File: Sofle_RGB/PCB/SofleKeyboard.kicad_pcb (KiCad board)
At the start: 2 copper layers, 143.4 x 111.8 mm, 97 parts, among them J1 LED, J2 4PIN, J3 OLED, J4 key leds, J5 backlight sel, J6 indicator bypass, P1 i2c_pin, P2 i2c_pin, SW1 SW_PUSH-MX_W_LED, SW10 SW_PUSH-MX_W_LED, SW11 SW_PUSH-MX_W_LED, SW12 SW_PUSH-MX_W_LED, SW13 SW_PUSH-MX_W_LED, SW14 SW_PUSH-MX_W_LED, SW15 SW_PUSH-MX_W_LED, SW16 SW_PUSH-MX_W_LED, SW17 SW_PUSH-MX_W_LED, SW18 SW_PUSH-MX_W_LED, SW19 SW_PUSH-MX_W_LED, SW2 SW_PUSH-MX_W_LED, SW20 SW_PUSH-MX_W_LED, SW21 SW_PUSH-MX_W_LED, SW22 SW_PUSH-MX_W_LED, SW23 SW_PUSH-MX_W_LED, SW24 SW_PUSH-MX_W_LED, SW25 Rotary_Encoder_Switch, SW26 SW_PUSH-MX_W_LED, SW27 SW_PUSH-MX_W_LED, SW28 SW_PUSH-MX_W_LED, SW29 SW_PUSH-MX_W_LED, SW3 SW_PUSH-MX_W_LED, SW30 SW_PUSH-MX_W_LED, SW4 SW_PUSH-MX_W_LED, SW5 SW_PUSH-MX_W_LED, SW6 SW_PUSH-MX_W_LED, SW7 SW_PUSH-MX_W_LED, SW8 SW_PUSH-MX_W_LED, SW9 SW_PUSH-MX_W_LED, U1 ProMicro

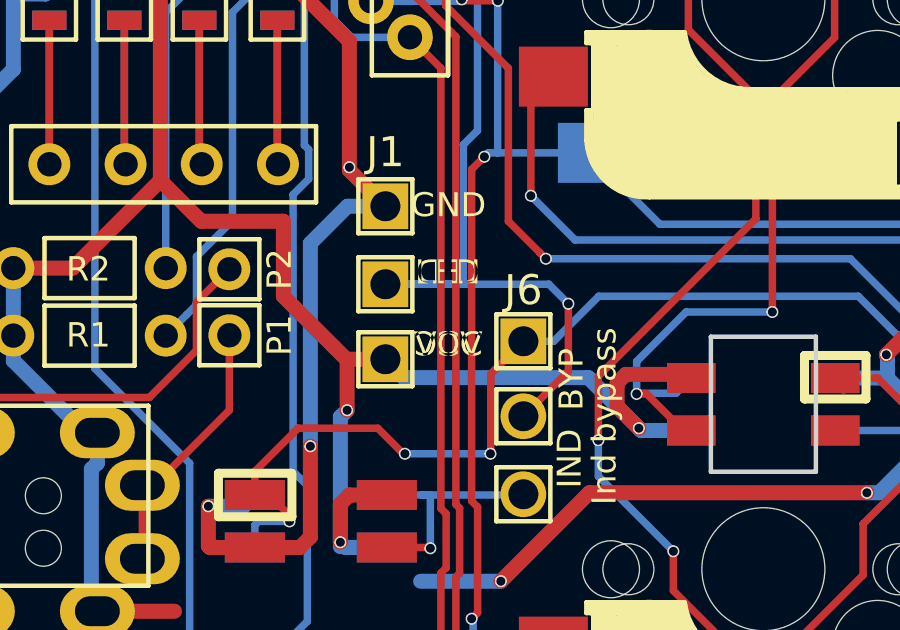
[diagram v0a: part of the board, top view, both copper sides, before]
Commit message: Fix labels for the RGB connector.
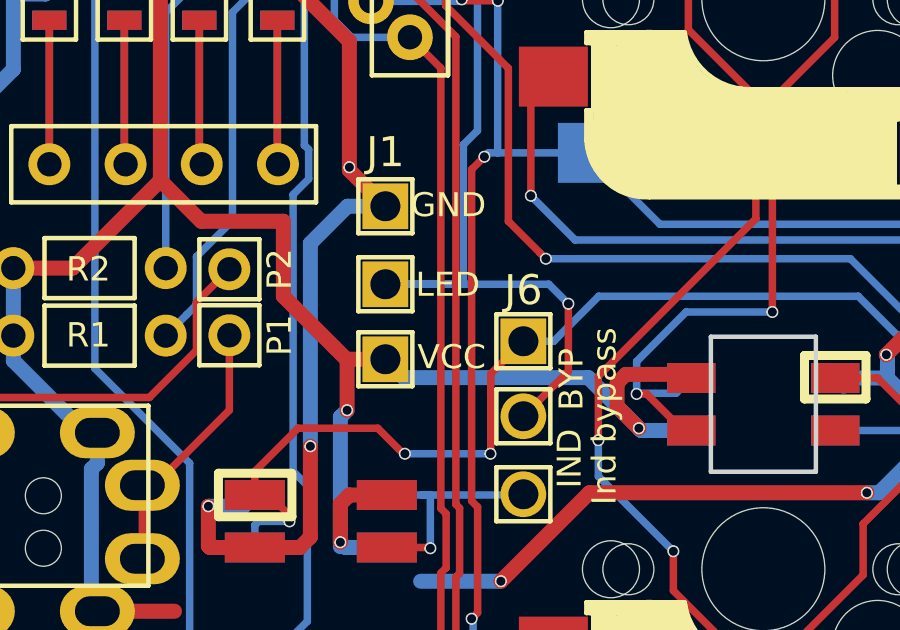
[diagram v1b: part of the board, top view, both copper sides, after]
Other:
- board text removed: "LED"
- board text removed: "VCC"
